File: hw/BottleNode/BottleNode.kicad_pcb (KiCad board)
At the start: 2 copper layers, 29 x 40 mm, 16 parts, among them J1 Conn_01x03_Pin, J2 Conn_01x02_Pin

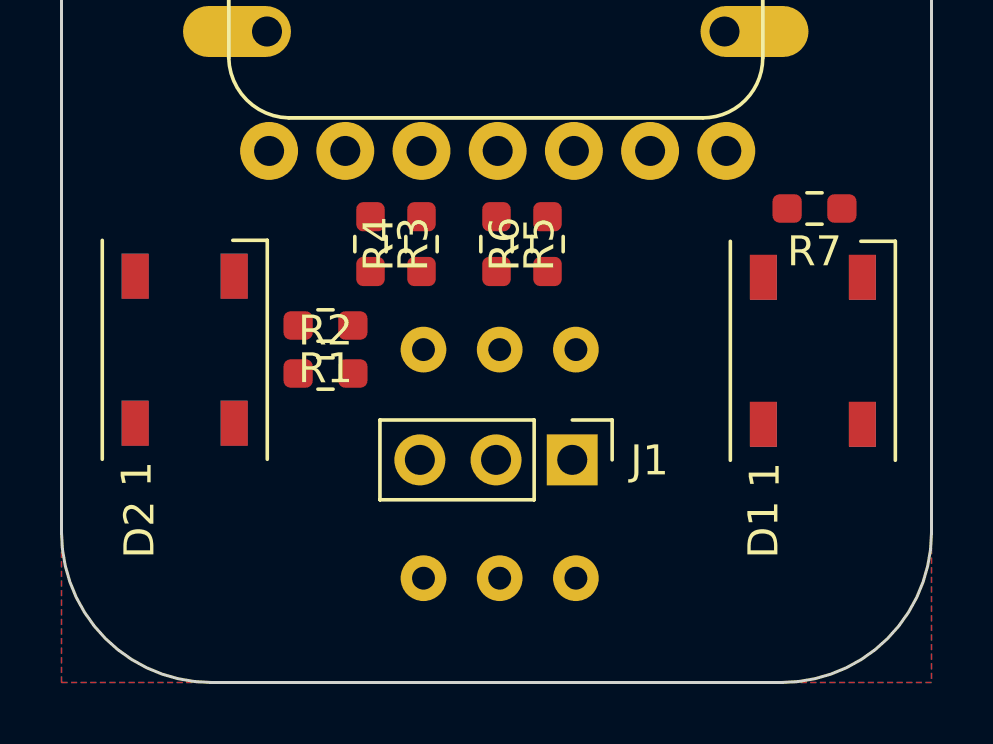
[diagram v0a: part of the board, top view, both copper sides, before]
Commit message: schematic and code fragments now agree on pinouts
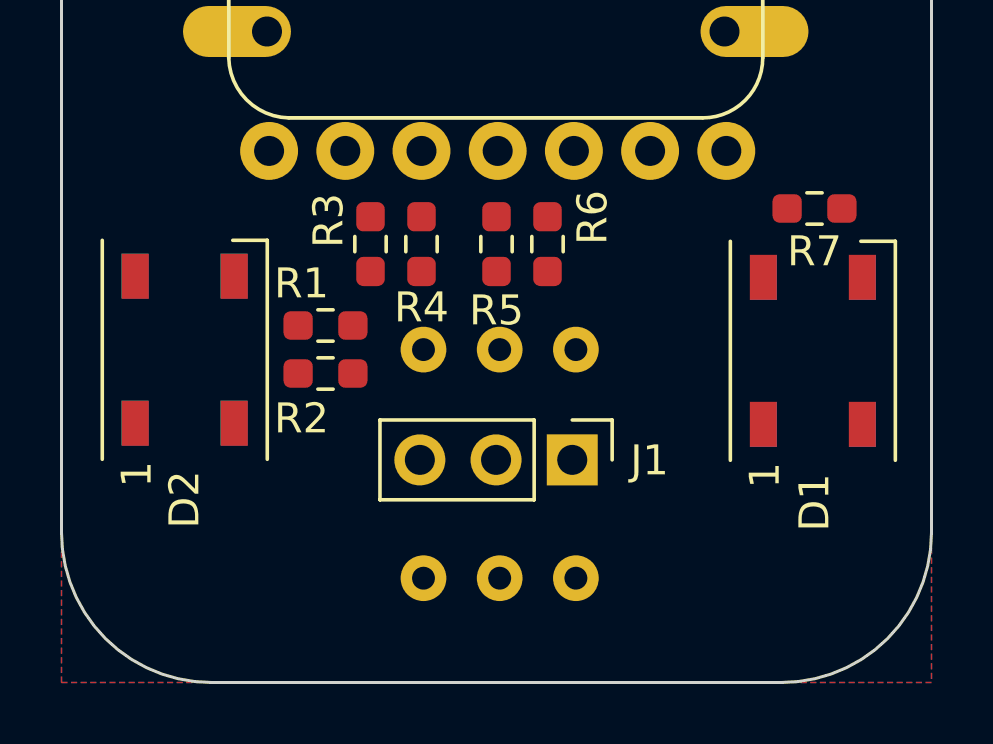
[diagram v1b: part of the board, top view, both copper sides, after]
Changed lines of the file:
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@@
     (property "ki_keywords" "R res resistor")
     (attr smd)
-    (fp_text reference "R2" (at 0 -1.43) (layer "F.SilkS")
+    (fp_text reference "R2" (at -0.8 1.5) (layer "F.SilkS")
         (effects (font (size 1 1) (thickness 0.15)))
     )
@@
     (property "ki_keywords" "R res resistor")
     (attr smd)
-    (fp_text reference "R1" (at 0 -1.43) (layer "F.SilkS")
+    (fp_text reference "R1" (at 0.8 1.4) (layer "F.SilkS")
         (effects (font (size 1 1) (thickness 0.15)))
     )
@@
     (property "ki_keywords" "R res resistor")
     (attr smd)
-    (fp_text reference "R6" (at 0 -1.43 90) (layer "F.SilkS")
+    (fp_text reference "R6" (at 0.8875 1.5 90) (layer "F.SilkS")
         (effects (font (size 1 1) (thickness 0.15)))
     )
@@
     (property "ki_keywords" "RGB LED NeoPixel addressable")
     (attr smd)
-    (fp_text reference "D2" (at -5.989551 -1.509112 90) (layer "F.SilkS")
+    (fp_text reference "D2" (at -4.989551 -0.009112 90) (layer "F.SilkS")
         (effects (font (size 1 1) (thickness 0.15)))
     )
@@
     (property "ki_keywords" "RGB LED NeoPixel addressable")
     (attr smd)
-    (fp_text reference "D1" (at -5.957244 -1.644796 90) (layer "F.SilkS")
+    (fp_text reference "D1" (at -5.057244 0.055204 90) (layer "F.SilkS")
         (effects (font (size 1 1) (thickness 0.15)))
     )
@@
     (fp_arc (start -6.9 10.5) (mid -8.301423 9.901423) (end -8.9 8.5)
       (stroke (width 0.12) (type solid)) (layer "F.SilkS"))
-    (fp_arc (start 6.9 -10.5) (mid 8.301492 -9.901492) (end 8.9 -8.5)
+    (fp_arc (start 6.9 -10.5) (mid 8.301494 -9.901494) (end 8.9 -8.5)
       (stroke (width 0.12) (type solid)) (layer "F.SilkS"))
     (fp_arc (start 8.9 8.5) (mid 8.314214 9.914214) (end 6.9 10.5)
@@
     (property "ki_keywords" "R res resistor")
     (attr smd)
-    (fp_text reference "R5" (at 0 -1.43 90) (layer "F.SilkS")
+    (fp_text reference "R5" (at 2.2125 0 -180) (layer "F.SilkS")
         (effects (font (size 1 1) (thickness 0.15)))
     )
@@
     (property "ki_keywords" "R res resistor")
     (attr smd)
-    (fp_text reference "R4" (at 0 -1.43 90) (layer "F.SilkS")
+    (fp_text reference "R4" (at -2.1125 0 180) (layer "F.SilkS")
         (effects (font (size 1 1) (thickness 0.15)))
     )
@@
     (property "ki_keywords" "R res resistor")
     (attr smd)
-    (fp_text reference "R3" (at 0 -1.43 90) (layer "F.SilkS")
+    (fp_text reference "R3" (at -0.7875 1.4 90) (layer "F.SilkS")
         (effects (font (size 1 1) (thickness 0.15)))
     )
@@
     (attr through_hole)
     (fp_text reference "U2" (at 0 0.5 180 unlocked) (layer "B.SilkS")
-        (effects (font (size 1 1) (thickness 0.1)) (justify mirror))
-    )
-    (fp_text value "~" (at 0 -7.62 180 unlocked) (layer "B.Fab")
-        (effects (font (size 1 1) (thickness 0.15)) (justify mirror))
-    )
-    (fp_text user "${REFERENCE}" (at -5.79 -6.26 180 unlocked) (layer "B.Fab")
-        (effects (font (size 1 1) (thickness 0.15)) (justify mirror))
+        (effects (font (size 0.762 0.762) (thickness 0.127)) (justify mirror))
+    )
+    (fp_text value "~" (at 0 -7.62 180 unlocked) (layer "B.SilkS")
+        (effects (font (size 0.762 0.762) (thickness 0.127)) (justify mirror))
+    )
+    (fp_text user "LR" (at -2.54 -5.88162 180 unlocked) (layer "B.SilkS")
+        (effects (font (size 0.762 0.762) (thickness 0.127)) (justify bottom mirror))
+    )
+    (fp_text user "SCK" (at 2.54 -5.824517 180 unlocked) (layer "B.SilkS")
+        (effects (font (size 0.762 0.762) (thickness 0.127)) (justify bottom mirror))
+    )
+    (fp_text user "VDD" (at 0 5.900654 unlocked) (layer "B.SilkS")
+        (effects (font (size 0.762 0.762) (thickness 0.127)) (justify bottom mirror))
+    )
+    (fp_text user "${REFERENCE}" (at 0 7.62 180 unlocked) (layer "B.SilkS")
+        (effects (font (size 0.762 0.762) (thickness 0.127)) (justify mirror))
+    )
+    (fp_text user "GND" (at -2.569639 5.805482 unlocked) (layer "B.SilkS")
+        (effects (font (size 0.762 0.762) (thickness 0.127)) (justify bottom mirror))
+    )
+    (fp_text user "WS" (at 0 -5.843551 180 unlocked) (layer "B.SilkS")
+        (effects (font (size 0.762 0.762) (thickness 0.127)) (justify bottom mirror))
+    )
+    (fp_text user "SD" (at 2.512536 5.957757 unlocked) (layer "B.SilkS")
+        (effects (font (size 0.762 0.762) (thickness 0.127)) (justify bottom mirror))
     )
     (fp_circle (center 0 0) (end 6.985 0)
@@
     (property "ki_keywords" "RGB LED NeoPixel addressable")
     (attr smd)
-    (fp_text reference "D4" (at -6.15 1.65 90) (layer "B.SilkS")
+    (fp_text reference "D4" (at -5.05 0.15 90) (layer "B.SilkS")
         (effects (font (size 1 1) (thickness 0.15)) (justify mirror))
     )
@@
     (property "ki_keywords" "RGB LED NeoPixel addressable")
     (attr smd)
-    (fp_text reference "D3" (at -5.9 1.7 90) (layer "B.SilkS")
+    (fp_text reference "D3" (at -5 0 90) (layer "B.SilkS")
         (effects (font (size 1 1) (thickness 0.15)) (justify mirror))
     )
@@
     (fp_arc (start 6.410284 -9.521063) (mid 8.206334 -8.777113) (end 8.950284 -6.981063)
       (stroke (width 0.05) (type solid)) (layer "B.SilkS"))
-    (fp_arc (start 8.950284 6.988937) (mid 8.206337 8.784992) (end 6.410284 9.528937)
+    (fp_arc (start 8.950284 6.988937) (mid 8.206339 8.784995) (end 6.410284 9.528937)
       (stroke (width 0.05) (type solid)) (layer "B.SilkS"))
     (fp_circle (center -4.699 3.908) (end -5.4807 3.908)

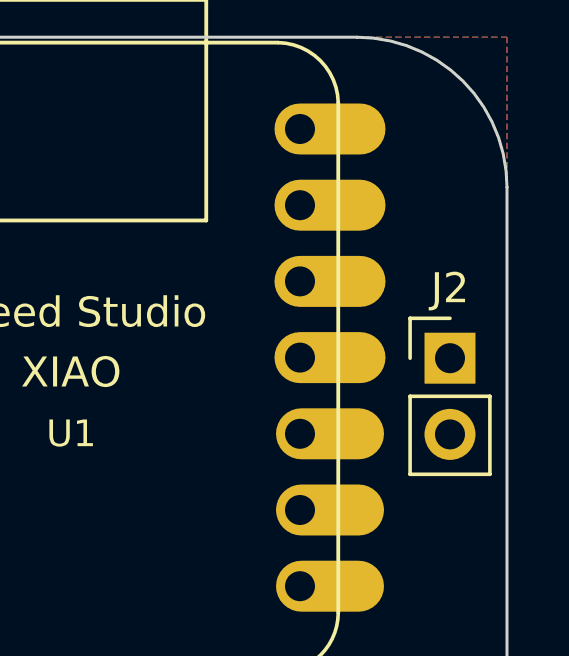
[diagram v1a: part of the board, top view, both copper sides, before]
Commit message: swap SPKR_POWER/TOUCH_PIN in AllInOne_test/sch/pcb
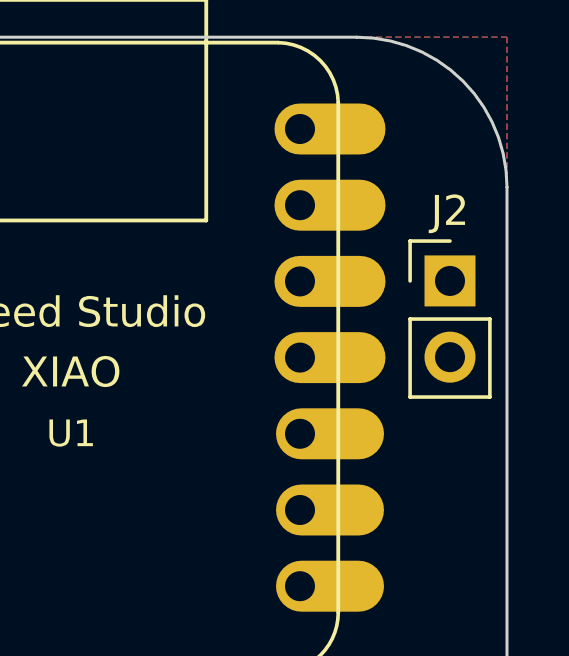
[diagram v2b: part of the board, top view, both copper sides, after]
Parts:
- R1: value DNP -> 0
- R2, R3, R6, R7: value DNP -> DNI
- moved J2 2.58 mm to (112.1, 74.1)
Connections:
- U1 pad 10: /PROX_ELECTRODE -> /SPKR_POWER
- U1 pad 11: /SPKR_POWER -> /PROX_ELECTRODE
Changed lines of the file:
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@@
         (effects (font (size 1 1) (thickness 0.15)))
     )
-    (fp_text value "DNP" (at 0 1.43) (layer "F.Fab")
+    (fp_text value "DNI" (at 0 1.43) (layer "F.Fab")
         (effects (font (size 1 1) (thickness 0.15)))
     )
@@
         (effects (font (size 1 1) (thickness 0.15)))
     )
-    (fp_text value "DNP" (at 0 1.43) (layer "F.Fab")
+    (fp_text value "0" (at 0 1.43) (layer "F.Fab")
         (effects (font (size 1 1) (thickness 0.15)))
     )
@@
         (effects (font (size 1 1) (thickness 0.15)))
     )
-    (fp_text value "DNP" (at 0 1.43 90) (layer "F.Fab")
+    (fp_text value "DNI" (at 0 1.43 90) (layer "F.Fab")
         (effects (font (size 1 1) (thickness 0.15)))
     )
@@
         (effects (font (size 1 1) (thickness 0.15)))
     )
-    (fp_text value "DNP" (at 0 1.43) (layer "F.Fab")
+    (fp_text value "DNI" (at 0 1.43) (layer "F.Fab")
         (effects (font (size 1 1) (thickness 0.15)))
     )
@@
       (net 3 "/LED_DIN") (pinfunction "AD8_GT7_SCK") (pintype "passive"))
     (pad "10" thru_hole oval locked (at 7.625 2.54) (size 3.6 1.7) (drill 1 (offset 1 0)) (layers "*.Cu" "*.Mask")
-      (net 18 "/PROX_ELECTRODE") (pinfunction "AD9_GT8_MISO") (pintype "passive"))
+      (net 6 "/SPKR_POWER") (pinfunction "AD9_GT8_MISO") (pintype "passive"))
     (pad "11" thru_hole oval locked (at 7.625 0) (size 3.7 1.7) (drill 1 (offset 1 0)) (layers "*.Cu" "*.Mask")
-      (net 6 "/SPKR_POWER") (pinfunction "AD10_GT9_MOSI") (pintype "passive"))
+      (net 18 "/PROX_ELECTRODE") (pinfunction "AD10_GT9_MOSI") (pintype "passive"))
     (pad "12" thru_hole oval locked (at 7.625 -2.54) (size 3.7 1.7) (drill 1 (offset 1 0)) (layers "*.Cu" "*.Mask")
       (net 15 "+3.3V") (pinfunction "3V3") (pintype "power_out"))
@@
         (effects (font (size 1 1) (thickness 0.15)))
     )
-    (fp_text value "DNP" (at 0 1.43 90) (layer "F.Fab")
+    (fp_text value "DNI" (at 0 1.43 90) (layer "F.Fab")
         (effects (font (size 1 1) (thickness 0.15)))
     )
@@
   )
   (footprint "Connector_PinHeader_2.54mm:PinHeader_1x02_P2.54mm_Vertical" (layer "F.Cu")
-    (at 112.1 76.7)
+    (at 112.1 74.125)
     (descr "Through hole straight pin header, 1x02, 2.54mm pitch, single row")
     (tags "Through hole pin header THT 1x02 2.54mm single row")
@@
         (effects (font (size 1 1) (thickness 0.15)))
     )
-    (fp_text value "Conn_01x02_Pin" (at 0 4.87) (layer "F.Fab")
+    (fp_text value "Conn_01x02_Pin" (at 0 4.87) (layer "F.Fab") hide
         (effects (font (size 1 1) (thickness 0.15)))
     )
@@
     (fp_arc (start 6.410284 -9.521063) (mid 8.206334 -8.777113) (end 8.950284 -6.981063)
       (stroke (width 0.05) (type solid)) (layer "B.SilkS"))
-    (fp_arc (start 8.950284 6.988937) (mid 8.206339 8.784995) (end 6.410284 9.528937)
+    (fp_arc (start 8.950284 6.988937) (mid 8.20634 8.784993) (end 6.410284 9.528937)
       (stroke (width 0.05) (type solid)) (layer "B.SilkS"))
     (fp_circle (center -4.699 3.908) (end -5.4807 3.908)

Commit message: rev 1.1 of schematic and PCB layout with BOM
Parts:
- added C1: 10nF, BottleNode:C_0603_1608Metric_Pad1.08x0.95mm_HandSolder, F.Cu at (101.1, 77.4)
- added C2: 10nF, BottleNode:C_0603_1608Metric_Pad1.08x0.95mm_HandSolder, F.Cu at (101.1, 101.3)
- added C3: 10nF, BottleNode:C_0603_1608Metric_Pad1.08x0.95mm_HandSolder, B.Cu at (112.6, 101.3)
- added C4: 10nF, BottleNode:C_0603_1608Metric_Pad1.08x0.95mm_HandSolder, B.Cu at (112.7, 77.3)
- added C5: 1uF, BottleNode:C_0603_1608Metric_Pad1.08x0.95mm_HandSolder, F.Cu at (106.7, 97.8)
- added J3: Conn_01x02_Pin, BottleNode:PinHeader_1x02_P2.54mm_Vertical, F.Cu at (90.4, 80.2)
- added R8: 100k, BottleNode:R_0603_1608Metric_Pad0.98x0.95mm_HandSolder, F.Cu at (122.8, 86.3)
- D1, D3: footprint LED_SMD:LED_WS2812B_PLCC4_5.0x5.0mm_P3.2mm -> BottleNode:LED_WS2812B_PLCC4_5.0x5.0mm_P3.2mm
- D2: footprint LED_SMD:LED_WS2812B_PLCC4_5.0x5.0mm_P3.2mm -> BottleNode:LED_WS2812B_PLCC4_5.0x5.0mm_P3.2mm; moved to B.Cu
- D4: footprint LED_SMD:LED_WS2812B_PLCC4_5.0x5.0mm_P3.2mm -> BottleNode:LED_WS2812B_PLCC4_5.0x5.0mm_P3.2mm; moved to F.Cu
- J1: footprint Connector_PinHeader_2.54mm:PinHeader_1x03_P2.54mm_Vertical -> BottleNode:PinHeader_1x03_P2.54mm_Vertical
- J2: footprint Connector_PinHeader_2.54mm:PinHeader_1x02_P2.54mm_Vertical -> BottleNode:PinHeader_1x02_P2.54mm_Vertical
- R1, R2, R3, R4, R5, R6, R7: footprint Resistor_SMD:R_0603_1608Metric_Pad0.98x0.95mm_HandSolder -> BottleNode:R_0603_1608Metric_Pad0.98x0.95mm_HandSolder
- U1: footprint Seeed Studio XIAO Series Library:XIAO-Generic-Hybrid-14P-2.54-21X17.8MM -> BottleNode:XIAO-Generic-Thruhole-14P-2.54-21X17.8MM
- U2: footprint BottleNode_footprints:INMP441_breakout -> BottleNode:INMP441_breakout
- U3: footprint BottleNode_footprints:MAX98357A_adafruit_breakout -> BottleNode:MAX98357A_adafruit_breakout; moved to F.Cu
- moved D2 23.9 mm to (107.0, 79.0), turned to 180 degrees
- moved J1 23.4 mm to (116.5, 80.2), turned to 90 degrees
- moved R2 23.2 mm to (116.9, 93.5), turned to 180 degrees
- moved R1 23.1 mm to (116.9, 95.2), turned to 0 degrees
- moved U2 19.9 mm to (118.0, 91.0), turned to 90 degrees
- moved D3 19.6 mm to (107.0, 103.0), turned to 180 degrees
- moved U3 19.1 mm to (116.0, 91.0), turned to -90 degrees
- moved J2 17.0 mm to (95.5, 77.8)
- moved D1 16.2 mm to (107.0, 79.0), turned to 180 degrees
- moved U1 14.9 mm to (95.5, 91.0), turned to 90 degrees
- moved R7 13.0 mm to (102.0, 80.0), turned to -90 degrees
- moved R3 11.2 mm to (106.0, 94.8), turned to 180 degrees
- moved R4 9.12 mm to (106.0, 93.1), turned to 0 degrees
- moved D4 8.62 mm to (107.0, 103.0), turned to 180 degrees
- moved R5 6.70 mm to (106.0, 89.7), turned to 180 degrees
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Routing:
- net Net-(D4-DOUT): track 0.00 -> 42.5 mm
- net /MIC_SD: track 0.00 -> 42.1 mm
- net /MIC_SCK: track 0.00 -> 41.1 mm
- net /MIC_WS: track 0.00 -> 36.3 mm
- net Net-(D2-DOUT): track 0.00 -> 25.4 mm
- net /SPKR_POWER: track 0.00 -> 23.1 mm
- net GND: track 0.00 -> 21.3 mm, vias 0 -> 5
- net /SPKR_LRC: track 0.00 -> 20.9 mm
- net /SPKR_BCLK: track 0.00 -> 17.2 mm
- net /SPKR_DIN: track 0.00 -> 13.6 mm
- net +3.3V: track 0.00 -> 8.36 mm, vias 0 -> 2
- net /LED_DIN: track 0.00 -> 5.70 mm
- net Net-(D1-DOUT): track 0.00 -> 5.33 mm, vias 0 -> 1
- net Net-(D3-DOUT): track 0.00 -> 5.17 mm, vias 0 -> 1
- net /SPKR_GAIN: track 0.00 -> 3.76 mm
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- added copper zone on F.Cu, net +3.3V
- removed copper zone on F.Cu, net GND
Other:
- board size 29 x 40 mm -> 40 x 30 mm
- board text added: "+3.3V plane"
- board text added: "BottleNode 1.1 ERP 3923"
- board text added: "GND plane"

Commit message: final tweaks on PCB v1.1
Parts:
- R1, R2: moved to B.Cu
- U1: value ~ -> XIAO ESP32S3
- U2: value ~ -> INMP441 breakout
- U3: value ~ -> MAX98357A breakout
- moved R1 5.39 mm to (112.5, 92.0), turned to 90 degrees
- moved R2 4.70 mm to (112.5, 95.3), turned to 90 degrees
- moved C4 1.91 mm to (114.6, 77.4)
- moved R8 1.37 mm to (121.8, 85.3), turned to -90 degrees
- moved C3 1.00 mm to (113.6, 101.4)
- moved U3 0.50 mm to (115.5, 91.0)
- moved C2 0.06 mm to (101.1, 101.4)
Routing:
- net +3.3V: track 8.36 -> 12.2 mm, vias 2 -> 3
- net /MIC_SD: track 42.1 -> 45.7 mm
- net /MIC_SCK: track 41.1 -> 44.4 mm
- net Net-(D2-DOUT): track 25.4 -> 27.6 mm
- net GND: track 21.3 -> 19.2 mm, vias 5 -> 4
- net Net-(D4-DOUT): track 42.5 -> 41.3 mm
- net /SPKR_POWER: track 23.1 -> 24.3 mm
- net /SPKR_DIN: track 13.6 -> 14.6 mm
- net /SPKR_BCLK: track 17.2 -> 18.1 mm
- net /SPKR_LRC: track 20.9 -> 21.8 mm

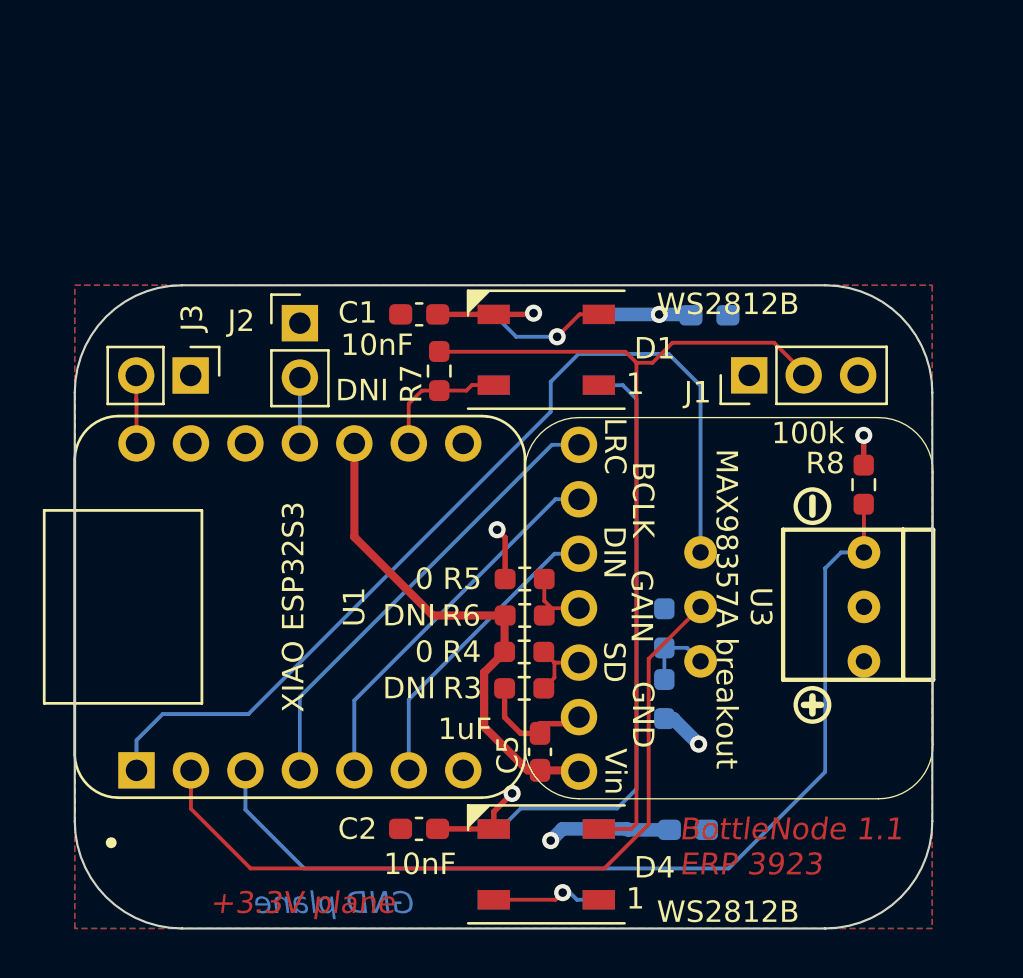
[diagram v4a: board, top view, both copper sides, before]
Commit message: rev 1.1.1 - move config resistors away from header
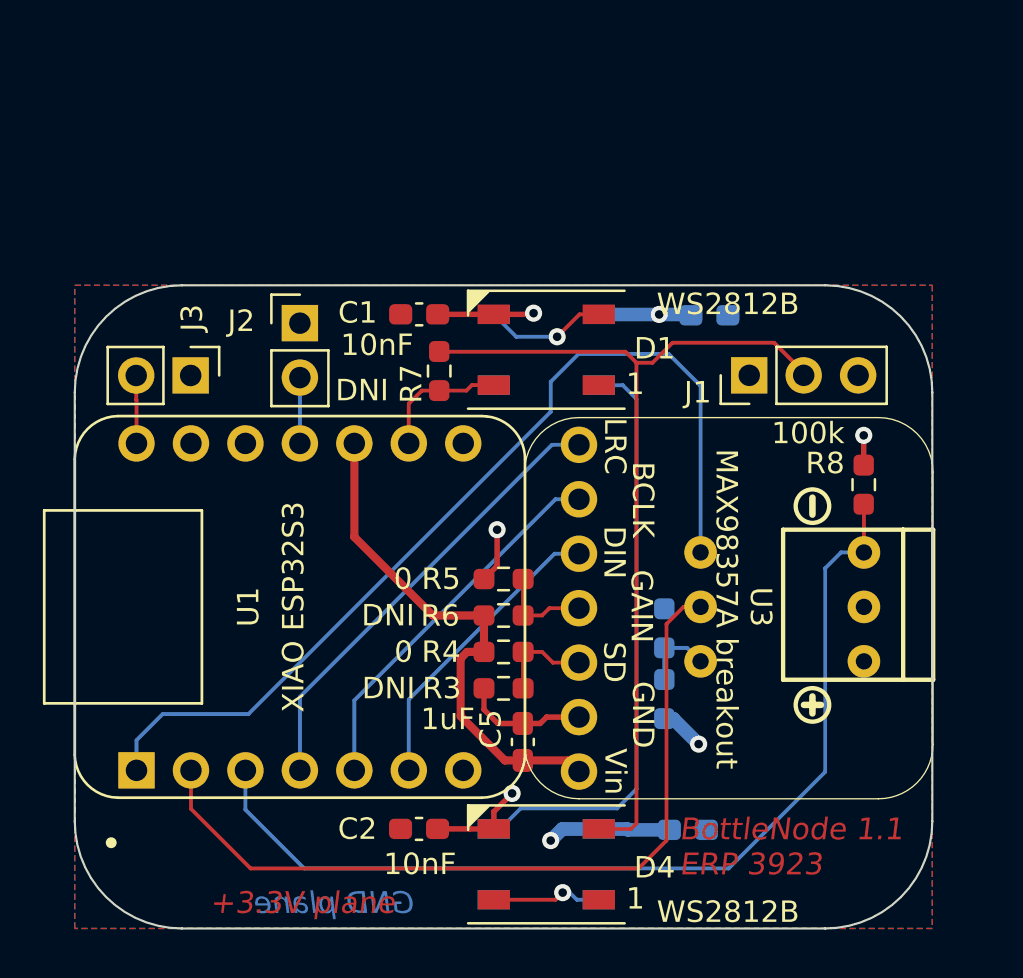
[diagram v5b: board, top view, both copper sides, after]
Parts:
- moved R5 0.99 mm to (105.0, 89.7)
- moved R6 0.99 mm to (105.0, 91.4)
- moved R3 0.96 mm to (105.0, 94.8)
- moved R4 0.96 mm to (105.0, 93.1)
- moved C5 0.92 mm to (105.9, 97.3)
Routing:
- net /MIC_WS: track 36.3 -> 37.7 mm
- net /SPKR_MODE: track 3.76 -> 4.51 mm
- net /SPKR_GAIN: track 3.76 -> 4.45 mm
